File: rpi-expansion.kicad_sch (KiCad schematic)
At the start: 15 parts, among them J7 PinHeader_2x20_P2.54mm_Drill1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, J8 JST_SH_1x4_SM04B-SRSS-TB-LF-SN, J9 JST_SH_1x4_SM04B-SRSS-TB-LF-SN, U8 NCP380LSNAJAAT1G

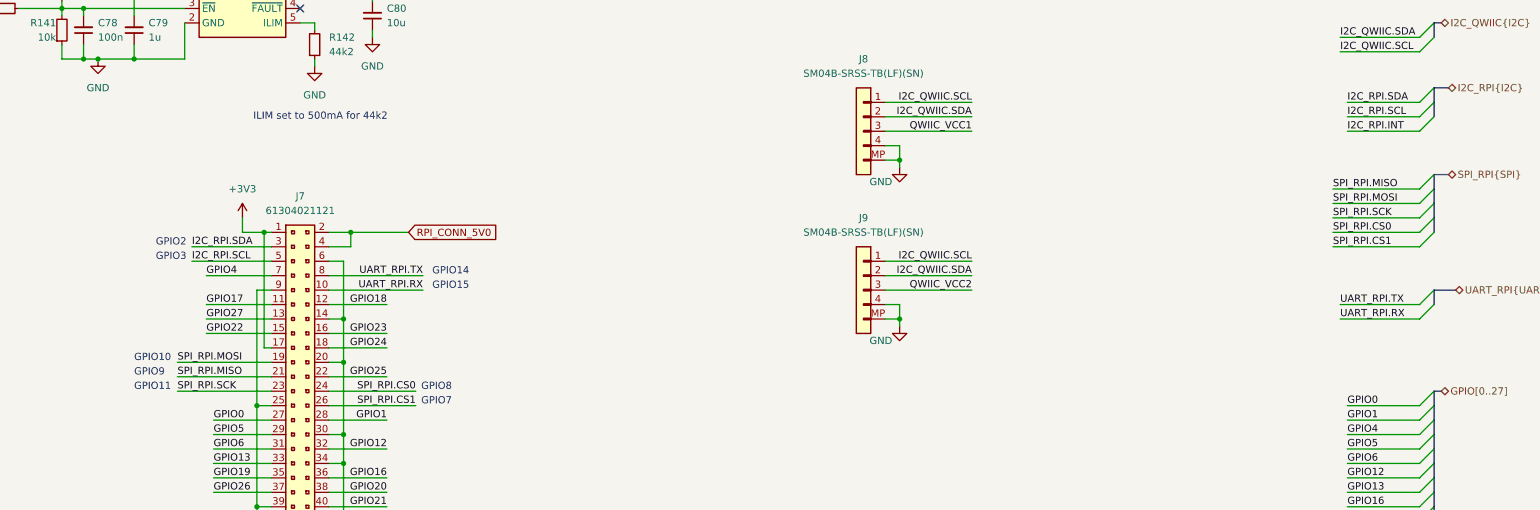
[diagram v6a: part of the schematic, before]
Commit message: [#95036] Connect PMOD pins to MCU
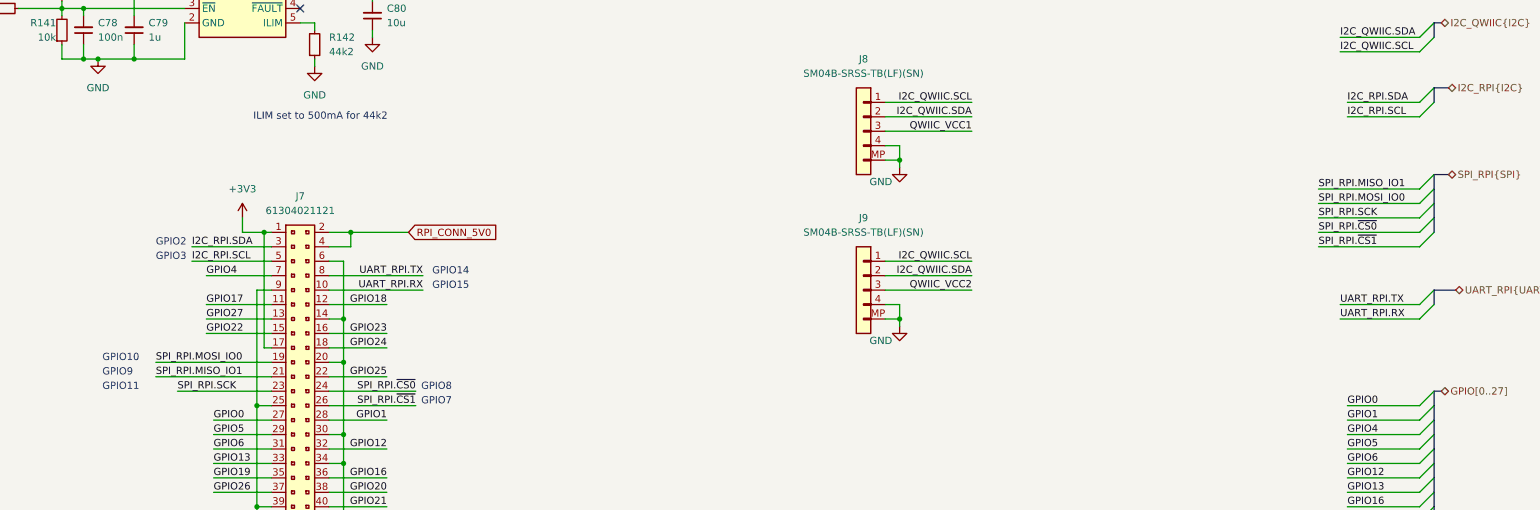
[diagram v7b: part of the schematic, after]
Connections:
- net SPI_RPI.CS0 renamed SPI_RPI.~{CS0}
- net SPI_RPI.CS1 renamed SPI_RPI.~{CS1}
- net SPI_RPI.MISO renamed SPI_RPI.MISO_IO1
- net SPI_RPI.MOSI renamed SPI_RPI.MOSI_IO0

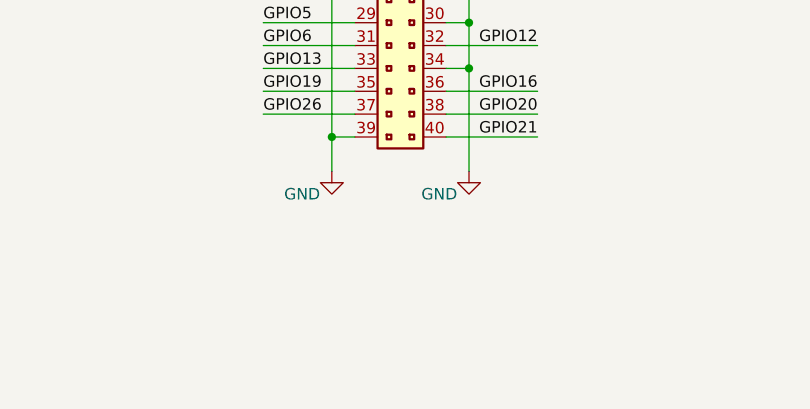
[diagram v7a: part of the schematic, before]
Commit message: [#95036] Add CAN bus subsheet
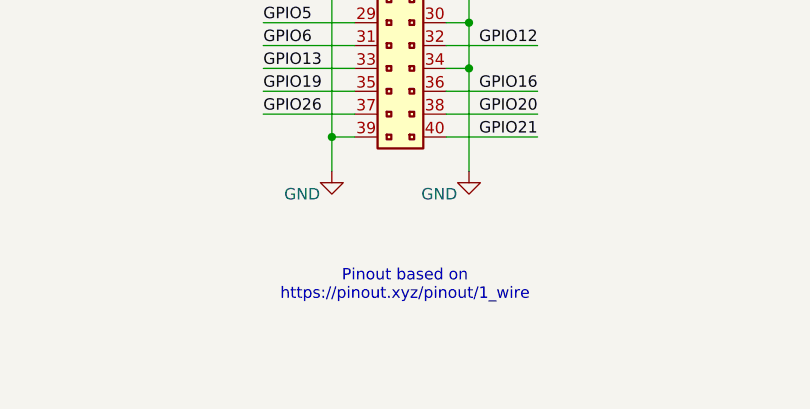
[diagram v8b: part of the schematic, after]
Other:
- note added: "Pinout based on https://pinout.xyz/pinout/1_wire"
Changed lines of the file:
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@@
 		(company "Antmicro")
+	)
+	(text "Pinout based on\nhttps://pinout.xyz/pinout/1_wire"
+		(exclude_from_sim no)
+		(at 152.908 190.5 0)
+		(effects
+			(font
+				(size 1.27 1.27)
+			)
+		)
 	)
 	(text "GPIO14"
